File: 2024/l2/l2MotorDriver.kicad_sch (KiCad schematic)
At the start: 45 parts, among them J4 Conn_01x02, J5 Conn_01x02, J6 Conn_01x02, J7 Conn_01x02, Q1 IRF540N, Q2 IRF540N, Q3 IRF540N, Q4 IRF540N, SW1 SW_SPDT, U1 VNH5019A-E, U2 VNH5019A-E, U3 VNH5019A-E, U4 VNH5019A-E

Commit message: 7/8 part_I
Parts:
- C1, C2, C3, C4: footprint (none) -> Capacitor_SMD:C_0603_1608Metric_Pad1.08x0.95mm_HandSolder
- R1, R10, R11, R12, R13, R14, R15, R16, R17, R18, R19, R2, R20, R21, R22, R23, R24, R25, R26, R27, R28, R3, R4, R5, R6, R7, R8, R9: footprint (none) -> Resistor_SMD:R_0603_1608Metric_Pad0.98x0.95mm_HandSolder
- SW1: footprint (none) -> Button_Switch_THT:SS12D00G3-2.5mm
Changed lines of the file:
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@@
 			)
 		)
-		(property "Footprint" ""
+		(property "Footprint" "Resistor_SMD:R_0603_1608Metric_Pad0.98x0.95mm_HandSolder"
 			(at 176.53 118.618 90)
 			(effects
@@
 			)
 		)
-		(property "Footprint" ""
+		(property "Footprint" "Resistor_SMD:R_0603_1608Metric_Pad0.98x0.95mm_HandSolder"
 			(at 175.26 61.468 90)
 			(effects
@@
 			)
 		)
-		(property "Footprint" ""
+		(property "Footprint" "Resistor_SMD:R_0603_1608Metric_Pad0.98x0.95mm_HandSolder"
 			(at 57.658 58.42 90)
 			(effects
@@
 			)
 		)
-		(property "Footprint" ""
+		(property "Footprint" "Resistor_SMD:R_0603_1608Metric_Pad0.98x0.95mm_HandSolder"
 			(at 58.928 123.19 90)
 			(effects
@@
 			)
 		)
-		(property "Footprint" ""
+		(property "Footprint" "Resistor_SMD:R_0603_1608Metric_Pad0.98x0.95mm_HandSolder"
 			(at 160.528 119.38 90)
 			(effects
@@
 			)
 		)
-		(property "Footprint" ""
+		(property "Footprint" "Button_Switch_THT:SS12D00G3-2.5mm"
 			(at 82.55 175.26 0)
 			(effects
@@
 			)
 		)
-		(property "Footprint" ""
+		(property "Footprint" "Resistor_SMD:R_0603_1608Metric_Pad0.98x0.95mm_HandSolder"
 			(at 61.468 123.19 90)
 			(effects
@@
 			)
 		)
-		(property "Footprint" ""
+		(property "Footprint" "Resistor_SMD:R_0603_1608Metric_Pad0.98x0.95mm_HandSolder"
 			(at 74.93 122.428 90)
 			(effects
@@
 			)
 		)
-		(property "Footprint" ""
+		(property "Footprint" "Resistor_SMD:R_0603_1608Metric_Pad0.98x0.95mm_HandSolder"
 			(at 71.12 55.118 90)
 			(effects
@@
 			)
 		)
-		(property "Footprint" ""
+		(property "Footprint" "Resistor_SMD:R_0603_1608Metric_Pad0.98x0.95mm_HandSolder"
 			(at 48.26 65.278 90)
 			(effects
@@
 			)
 		)
-		(property "Footprint" ""
+		(property "Footprint" "Resistor_SMD:R_0603_1608Metric_Pad0.98x0.95mm_HandSolder"
 			(at 159.258 59.69 90)
 			(effects
@@
 			)
 		)
-		(property "Footprint" ""
+		(property "Footprint" "Resistor_SMD:R_0603_1608Metric_Pad0.98x0.95mm_HandSolder"
 			(at 52.07 132.588 90)
 			(effects
@@
 			)
 		)
-		(property "Footprint" ""
+		(property "Footprint" "Resistor_SMD:R_0603_1608Metric_Pad0.98x0.95mm_HandSolder"
 			(at 71.12 57.658 90)
 			(effects
@@
 			)
 		)
-		(property "Footprint" ""
+		(property "Footprint" "Resistor_SMD:R_0603_1608Metric_Pad0.98x0.95mm_HandSolder"
 			(at 161.798 59.69 90)
 			(effects
@@
 			)
 		)
-		(property "Footprint" ""
+		(property "Footprint" "Resistor_SMD:R_0603_1608Metric_Pad0.98x0.95mm_HandSolder"
 			(at 74.93 119.888 90)
 			(effects
@@
 			)
 		)
-		(property "Footprint" ""
+		(property "Footprint" "Resistor_SMD:R_0603_1608Metric_Pad0.98x0.95mm_HandSolder"
 			(at 163.068 119.38 90)
 			(effects
@@
 			)
 		)
-		(property "Footprint" ""
+		(property "Footprint" "Resistor_SMD:R_0603_1608Metric_Pad0.98x0.95mm_HandSolder"
 			(at 152.4 66.548 90)
 			(effects
@@
 			)
 		)
-		(property "Footprint" ""
+		(property "Footprint" "Resistor_SMD:R_0603_1608Metric_Pad0.98x0.95mm_HandSolder"
 			(at 175.26 58.928 90)
 			(effects
@@
 			)
 		)
-		(property "Footprint" ""
+		(property "Footprint" "Resistor_SMD:R_0603_1608Metric_Pad0.98x0.95mm_HandSolder"
 			(at 153.67 128.778 90)
 			(effects
@@
 			)
 		)
-		(property "Footprint" ""
+		(property "Footprint" "Resistor_SMD:R_0603_1608Metric_Pad0.98x0.95mm_HandSolder"
 			(at 152.4 69.088 90)
 			(effects
@@
 			)
 		)
-		(property "Footprint" ""
+		(property "Footprint" "Resistor_SMD:R_0603_1608Metric_Pad0.98x0.95mm_HandSolder"
 			(at 153.67 126.238 90)
 			(effects
@@
 			)
 		)
-		(property "Footprint" ""
+		(property "Footprint" "Resistor_SMD:R_0603_1608Metric_Pad0.98x0.95mm_HandSolder"
 			(at 176.53 121.158 90)
 			(effects
@@
 			)
 		)
-		(property "Footprint" ""
+		(property "Footprint" "Capacitor_SMD:C_0603_1608Metric_Pad1.08x0.95mm_HandSolder"
 			(at 119.0752 49.53 0)
 			(effects
@@
 			)
 		)
-		(property "Footprint" ""
+		(property "Footprint" "Resistor_SMD:R_0603_1608Metric_Pad0.98x0.95mm_HandSolder"
 			(at 48.26 67.818 90)
 			(effects
@@
 			)
 		)
-		(property "Footprint" ""
+		(property "Footprint" "Resistor_SMD:R_0603_1608Metric_Pad0.98x0.95mm_HandSolder"
 			(at 175.26 56.388 90)
 			(effects
@@
 			)
 		)
-		(property "Footprint" ""
+		(property "Footprint" "Resistor_SMD:R_0603_1608Metric_Pad0.98x0.95mm_HandSolder"
 			(at 52.07 130.048 90)
 			(effects
@@
 			)
 		)
-		(property "Footprint" ""
+		(property "Footprint" "Resistor_SMD:R_0603_1608Metric_Pad0.98x0.95mm_HandSolder"
 			(at 55.118 58.42 90)
 			(effects
@@
 			)
 		)
-		(property "Footprint" ""
+		(property "Footprint" "Capacitor_SMD:C_0603_1608Metric_Pad1.08x0.95mm_HandSolder"
 			(at 224.4852 110.49 0)
 			(effects
@@
 			)
 		)
-		(property "Footprint" ""
+		(property "Footprint" "Resistor_SMD:R_0603_1608Metric_Pad0.98x0.95mm_HandSolder"
 			(at 176.53 116.078 90)
 			(effects
@@
 			)
 		)
-		(property "Footprint" ""
+		(property "Footprint" "Resistor_SMD:R_0603_1608Metric_Pad0.98x0.95mm_HandSolder"
 			(at 71.12 60.198 90)
 			(effects
@@
 			)
 		)
-		(property "Footprint" ""
+		(property "Footprint" "Resistor_SMD:R_0603_1608Metric_Pad0.98x0.95mm_HandSolder"
 			(at 74.93 124.968 90)
 			(effects
@@
 			)
 		)
-		(property "Footprint" ""
+		(property "Footprint" "Capacitor_SMD:C_0603_1608Metric_Pad1.08x0.95mm_HandSolder"
 			(at 223.2152 50.8 0)
 			(effects
@@
 			)
 		)
-		(property "Footprint" ""
+		(property "Footprint" "Capacitor_SMD:C_0603_1608Metric_Pad1.08x0.95mm_HandSolder"
 			(at 122.8852 114.3 0)
 			(effects

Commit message: 7/8 final
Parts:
- renumbered Q2 to Q1, Q1 to Q2
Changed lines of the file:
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@@
 		(dnp no)
 		(fields_autoplaced yes)
-		(property "Reference" "Q1"
+		(property "Reference" "Q2"
 			(at 194.31 31.75 90)
 			(effects
@@
 			(project "l2"
 				(path "/6e23b0dc-b56a-4591-91ab-7fa94dae0df0/07f2b048-6ef5-43cf-a929-1dfccb679372"
-					(reference "Q1")
+					(reference "Q2")
 					(unit 1)
 				)
@@
 		(dnp no)
 		(fields_autoplaced yes)
-		(property "Reference" "Q2"
+		(property "Reference" "Q1"
 			(at 90.17 30.48 90)
 			(effects
@@
 			(project "l2"
 				(path "/6e23b0dc-b56a-4591-91ab-7fa94dae0df0/07f2b048-6ef5-43cf-a929-1dfccb679372"
-					(reference "Q2")
-					(unit 1)
-				)
+					(reference "Q1")
+					(unit 1)
+				)

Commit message: 14/8 final
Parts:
- C1, C2, C3, C4: footprint Capacitor_SMD:C_0603_1608Metric_Pad1.08x0.95mm_HandSolder -> Capacitor_THT:CP_Radial_D8.0mm_P3.50mm
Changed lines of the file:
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@@
 			)
 		)
-		(property "Footprint" "Capacitor_SMD:C_0603_1608Metric_Pad1.08x0.95mm_HandSolder"
+		(property "Footprint" "Capacitor_THT:CP_Radial_D8.0mm_P3.50mm"
 			(at 119.0752 49.53 0)
 			(effects
@@
 			)
 		)
-		(property "Footprint" "Capacitor_SMD:C_0603_1608Metric_Pad1.08x0.95mm_HandSolder"
+		(property "Footprint" "Capacitor_THT:CP_Radial_D8.0mm_P3.50mm"
 			(at 224.4852 110.49 0)
 			(effects
@@
 			)
 		)
-		(property "Footprint" "Capacitor_SMD:C_0603_1608Metric_Pad1.08x0.95mm_HandSolder"
+		(property "Footprint" "Capacitor_THT:CP_Radial_D8.0mm_P3.50mm"
 			(at 223.2152 50.8 0)
 			(effects
@@
 			)
 		)
-		(property "Footprint" "Capacitor_SMD:C_0603_1608Metric_Pad1.08x0.95mm_HandSolder"
+		(property "Footprint" "Capacitor_THT:CP_Radial_D8.0mm_P3.50mm"
 			(at 122.8852 114.3 0)
 			(effects

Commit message: 16/8 final
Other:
- moved on the sheet: R10, R11, R8, R9
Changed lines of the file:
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@@
 	)
 	(junction
-		(at 54.61 54.61)
+		(at 49.53 54.61)
 		(diameter 0)
 		(color 0 0 0 0)
@@
 	)
 	(junction
-		(at 53.34 66.04)
+		(at 48.26 66.04)
 		(diameter 0)
 		(color 0 0 0 0)
@@
 	)
 	(junction
-		(at 55.88 63.5)
+		(at 50.8 63.5)
 		(diameter 0)
 		(color 0 0 0 0)
@@
 	)
 	(junction
-		(at 44.45 66.04)
+		(at 39.37 66.04)
 		(diameter 0)
 		(color 0 0 0 0)
@@
 	(wire
 		(pts
-			(xy 54.61 49.53) (xy 54.61 54.61)
+			(xy 49.53 49.53) (xy 49.53 54.61)
 		)
 		(stroke
@@
 	(wire
 		(pts
-			(xy 53.34 66.04) (xy 52.07 66.04)
+			(xy 48.26 66.04) (xy 46.99 66.04)
 		)
 		(stroke
@@
 	(wire
 		(pts
-			(xy 55.88 63.5) (xy 52.07 63.5)
+			(xy 50.8 63.5) (xy 46.99 63.5)
 		)
 		(stroke
@@
 	(wire
 		(pts
-			(xy 44.45 66.04) (xy 44.45 78.74)
+			(xy 39.37 66.04) (xy 39.37 78.74)
 		)
 		(stroke
@@
 	(wire
 		(pts
-			(xy 44.45 63.5) (xy 44.45 66.04)
+			(xy 39.37 63.5) (xy 39.37 66.04)
 		)
 		(stroke
@@
 	(wire
 		(pts
-			(xy 53.34 66.04) (xy 74.93 66.04)
+			(xy 48.26 66.04) (xy 74.93 66.04)
 		)
 		(stroke
@@
 	(wire
 		(pts
-			(xy 53.34 54.61) (xy 54.61 54.61)
+			(xy 48.26 54.61) (xy 49.53 54.61)
 		)
 		(stroke
@@
 	(wire
 		(pts
-			(xy 55.88 63.5) (xy 74.93 63.5)
-		)
-		(stroke
-			(width 0)
-			(type default)
-		)
-	)
-	(wire
-		(pts
-			(xy 59.69 58.42) (xy 67.31 58.42)
+			(xy 50.8 63.5) (xy 74.93 63.5)
 		)
 		(stroke
@@
 	(wire
 		(pts
-			(xy 44.45 78.74) (xy 87.63 78.74)
+			(xy 39.37 78.74) (xy 87.63 78.74)
 		)
 		(stroke
@@
 	(wire
 		(pts
-			(xy 55.88 62.23) (xy 55.88 63.5)
+			(xy 50.8 62.23) (xy 50.8 63.5)
 		)
 		(stroke
@@
 	(wire
 		(pts
-			(xy 53.34 62.23) (xy 53.34 66.04)
+			(xy 48.26 62.23) (xy 48.26 66.04)
 		)
 		(stroke
@@
 	(wire
 		(pts
-			(xy 54.61 54.61) (xy 55.88 54.61)
+			(xy 49.53 54.61) (xy 50.8 54.61)
 		)
 		(stroke
@@
 		)
 	)
-	(label "PWM_1"
-		(at 59.69 58.42 0)
-		(fields_autoplaced yes)
-		(effects
-			(font
-				(size 1.27 1.27)
-			)
-			(justify left bottom)
-		)
-	)
 	(label "MD"
 		(at 58.42 118.11 90)
@@
 	)
 	(label "MD"
-		(at 54.61 53.34 90)
+		(at 49.53 53.34 90)
 		(fields_autoplaced yes)
 		(effects
@@
 		)
 	)
+	(hierarchical_label "PWM_1"
+		(shape input)
+		(at 67.31 58.42 180)
+		(fields_autoplaced yes)
+		(effects
+			(font
+				(size 1.27 1.27)
+			)
+			(justify right)
+		)
+	)
 	(symbol
 		(lib_id "Connector_Generic:Conn_01x02")
@@
 	(symbol
 		(lib_id "Device:R")
-		(at 55.88 58.42 180)
+		(at 50.8 58.42 180)
 		(unit 1)
 		(exclude_from_sim no)
@@
 		(dnp no)
 		(property "Reference" "R11"
-			(at 57.15 59.436 0)
+			(at 52.07 59.436 0)
 			(effects
 				(font
@@
 		)
 		(property "Value" "3.3k"
-			(at 55.88 60.452 90)
+			(at 50.8 60.452 90)
 			(effects
 				(font
@@
 		)
 		(property "Footprint" "Resistor_SMD:R_0603_1608Metric_Pad0.98x0.95mm_HandSolder"
-			(at 57.658 58.42 90)
+			(at 52.578 58.42 90)
 			(effects
 				(font
@@
 		)
 		(property "Datasheet" "~"
-			(at 55.88 58.42 0)
+			(at 50.8 58.42 0)
 			(effects
 				(font
@@
 		)
 		(property "Description" "Resistor"
-			(at 55.88 58.42 0)
+			(at 50.8 58.42 0)
 			(effects
 				(font
@@
 	(symbol
 		(lib_id "Device:R")
-		(at 48.26 63.5 90)
+		(at 43.18 63.5 90)
 		(unit 1)
 		(exclude_from_sim no)
@@
 		(dnp no)
 		(property "Reference" "R8"
-			(at 48.26 61.468 90)
+			(at 43.18 61.468 90)
 			(effects
 				(font
@@
 		)
 		(property "Value" "1k"
-			(at 48.26 63.5 90)
+			(at 43.18 63.5 90)
 			(effects
 				(font
@@
 		)
 		(property "Footprint" "Resistor_SMD:R_0603_1608Metric_Pad0.98x0.95mm_HandSolder"
-			(at 48.26 65.278 90)
+			(at 43.18 65.278 90)
 			(effects
 				(font
@@
 		)
 		(property "Datasheet" "~"
-			(at 48.26 63.5 0)
+			(at 43.18 63.5 0)
 			(effects
 				(font
@@
 		)
 		(property "Description" "Resistor"
-			(at 48.26 63.5 0)
+			(at 43.18 63.5 0)
 			(effects
 				(font
@@
 	(symbol
 		(lib_id "Device:R")
-		(at 48.26 66.04 90)
+		(at 43.18 66.04 90)
 		(unit 1)
 		(exclude_from_sim no)
@@
 		(dnp no)
 		(property "Reference" "R9"
-			(at 48.26 68.326 90)
+			(at 43.18 68.326 90)
 			(effects
 				(font
@@
 		)
 		(property "Value" "1k"
-			(at 48.26 66.04 90)
+			(at 43.18 66.04 90)
 			(effects
 				(font
@@
 		)
 		(property "Footprint" "Resistor_SMD:R_0603_1608Metric_Pad0.98x0.95mm_HandSolder"
-			(at 48.26 67.818 90)
+			(at 43.18 67.818 90)
 			(effects
 				(font
@@
 		)
 		(property "Datasheet" "~"
-			(at 48.26 66.04 0)
+			(at 43.18 66.04 0)
 			(effects
 				(font
@@
 		)
 		(property "Description" "Resistor"
-			(at 48.26 66.04 0)
+			(at 43.18 66.04 0)
 			(effects
 				(font
@@
 	(symbol
 		(lib_id "Device:R")
-		(at 53.34 58.42 180)
+		(at 48.26 58.42 180)
 		(unit 1)
 		(exclude_from_sim no)
@@
 		(dnp no)
 		(property "Reference" "R10"
-			(at 48.26 59.69 0)
+			(at 43.18 59.69 0)
 			(effects
 				(font
@@
 		)
 		(property "Value" "3.3k"
-			(at 53.34 60.452 90)
+			(at 48.26 60.452 90)
 			(effects
 				(font
@@
 		)
 		(property "Footprint" "Resistor_SMD:R_0603_1608Metric_Pad0.98x0.95mm_HandSolder"
-			(at 55.118 58.42 90)
+			(at 50.038 58.42 90)
 			(effects
 				(font
@@
 		)
 		(property "Datasheet" "~"
-			(at 53.34 58.42 0)
+			(at 48.26 58.42 0)
 			(effects
 				(font
@@
 		)
 		(property "Description" "Resistor"
-			(at 53.34 58.42 0)
+			(at 48.26 58.42 0)
 			(effects
 				(font

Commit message: 21/8 final
about 10% done l2 pcb
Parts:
- J4: renamed from J5; footprint (none) -> Connector_AMASS:AMASS_XT30UPB-F_1x02_P5.0mm_Vertical
- J5: renamed from J4; footprint (none) -> Connector_AMASS:AMASS_XT30UPB-F_1x02_P5.0mm_Vertical
- J6, J7: footprint (none) -> Connector_AMASS:AMASS_XT30UPB-F_1x02_P5.0mm_Vertical

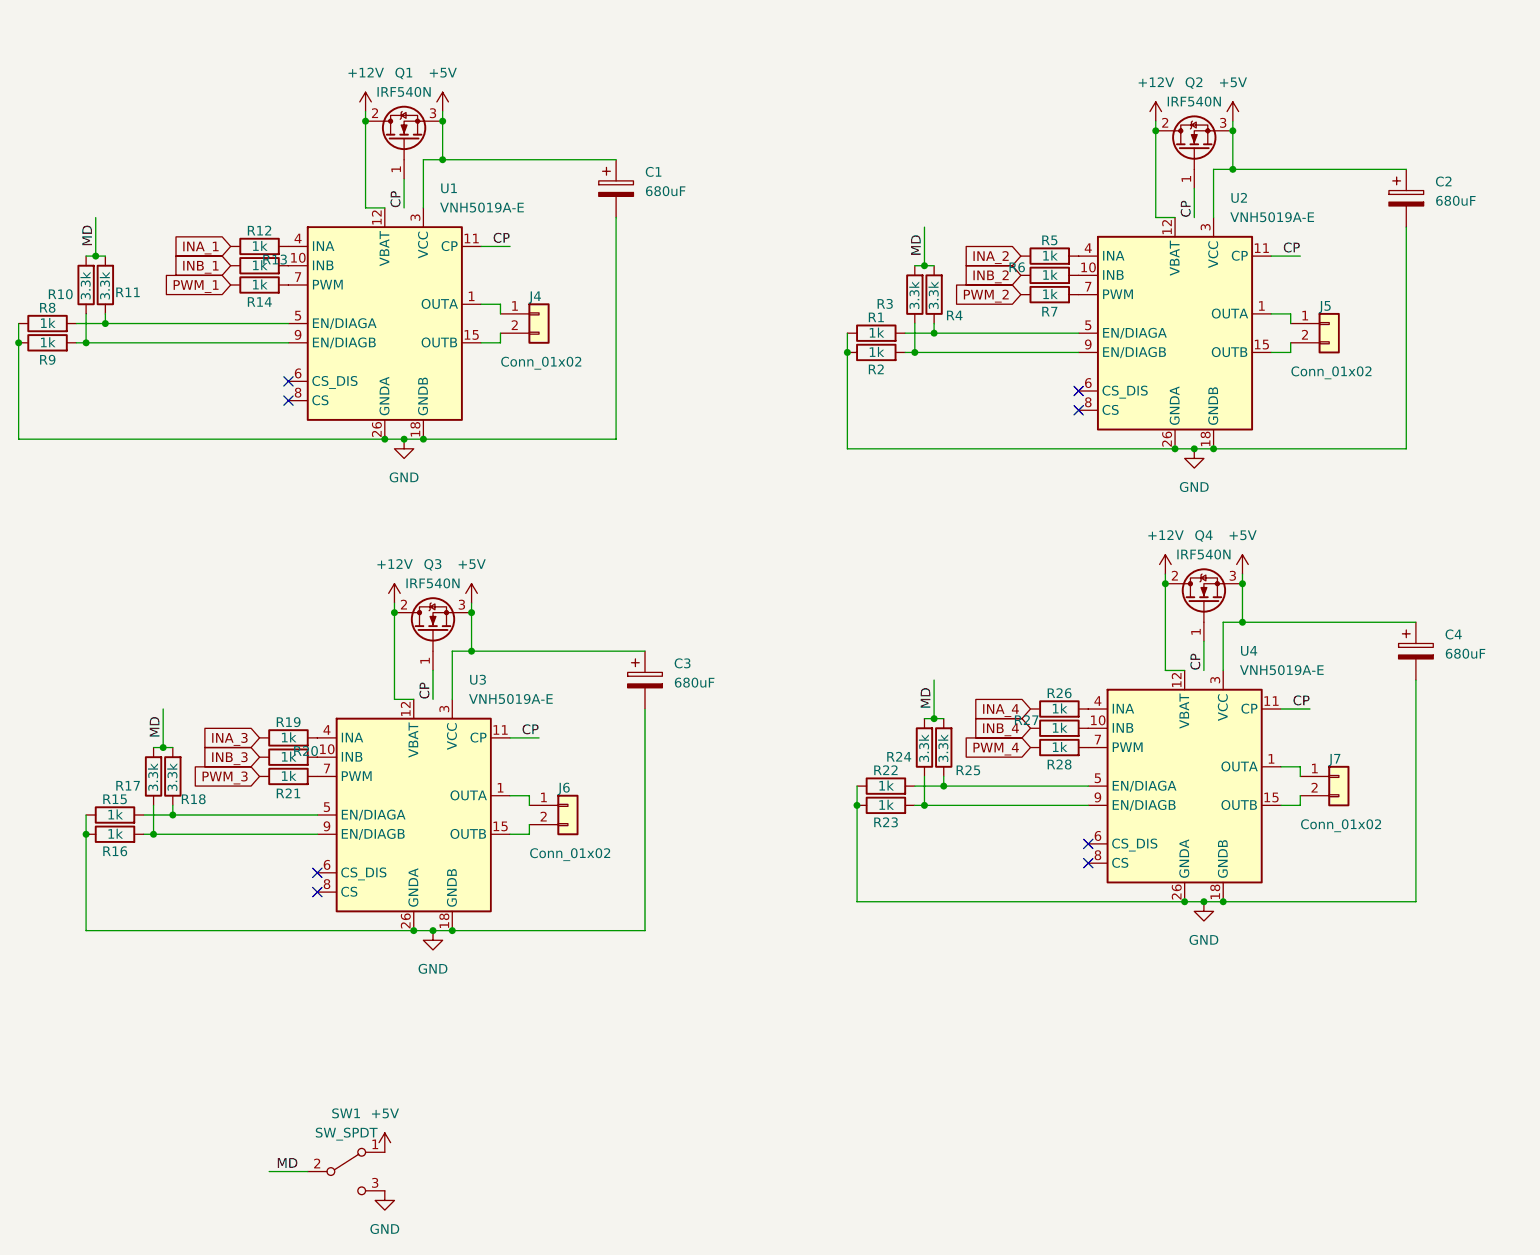
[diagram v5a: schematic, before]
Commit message: 28/8 final
resistors for motor driver removed as it was too cumbersome to do the traces and is also completely optional
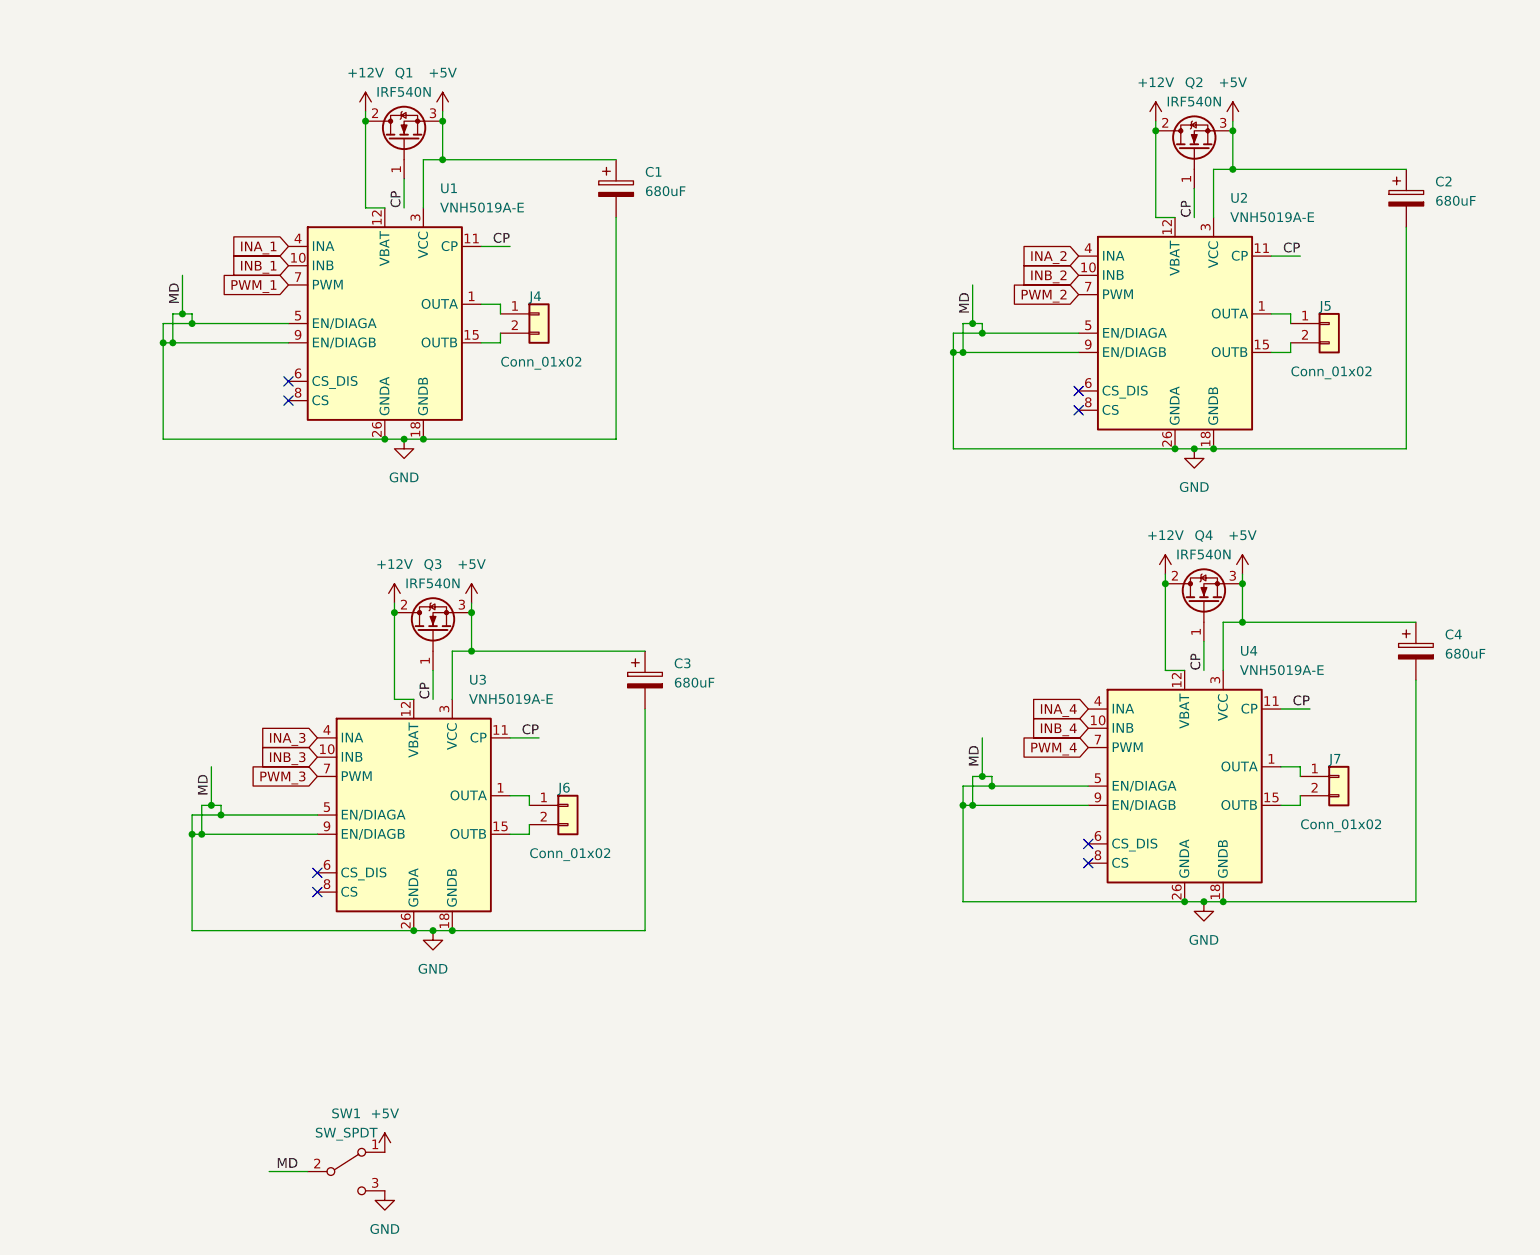
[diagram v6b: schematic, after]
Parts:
- removed R1, R12, R13, R14, R15, R16, R19, R2, R20, R21, R22, R23, R26, R27, R28, R5, R6, R7, R8, R9: 1k, Resistor_SMD:R_0603_1608Metric_Pad0.98x0.95mm_HandSolder, symbol Device:R
- removed R10, R11, R17, R18, R24, R25, R3, R4: 3.3k, Resistor_SMD:R_0603_1608Metric_Pad0.98x0.95mm_HandSolder, symbol Device:R
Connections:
- net MD is gone; now on net GND: SW1.2 (B)
- net GND: now also U1.5 (EN/DIAGA), U1.9 (EN/DIAGB), U2.5 (EN/DIAGA), U2.9 (EN/DIAGB), U3.5 (EN/DIAGA), U3.9 (EN/DIAGB), U4.5 (EN/DIAGA), U4.9 (EN/DIAGB)
- net INA_1: now also U1.4 (INA)
- net INA_2: now also U2.4 (INA)
- net INA_3: now also U3.4 (INA)
- net INA_4: now also U4.4 (INA)
- net INB_1: now also U1.10 (INB)
- net INB_2: now also U2.10 (INB)
- net INB_3: now also U3.10 (INB)
- net INB_4: now also U4.10 (INB)
- net PWM_1: now also U1.7 (PWM)
- net PWM_2: now also U2.7 (PWM)
- net PWM_3: now also U3.7 (PWM)
- net PWM_4: now also U4.7 (PWM)
